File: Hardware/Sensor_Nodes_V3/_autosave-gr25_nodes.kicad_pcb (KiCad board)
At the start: 4 copper layers, 22.1 x 70 mm, 72 parts, among them J1 Conn_01x06_Socket, J2 Conn_01x27_Socket, J3 Conn_01x27_Socket, Q1 S9013, U1 STM32F103C8Tx, U2 STM32G474RBTx, U3 MCP2542FDxMF, U4 MCP2542FDxMF, U5 AMS1117-3.3, U6 TPS563200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

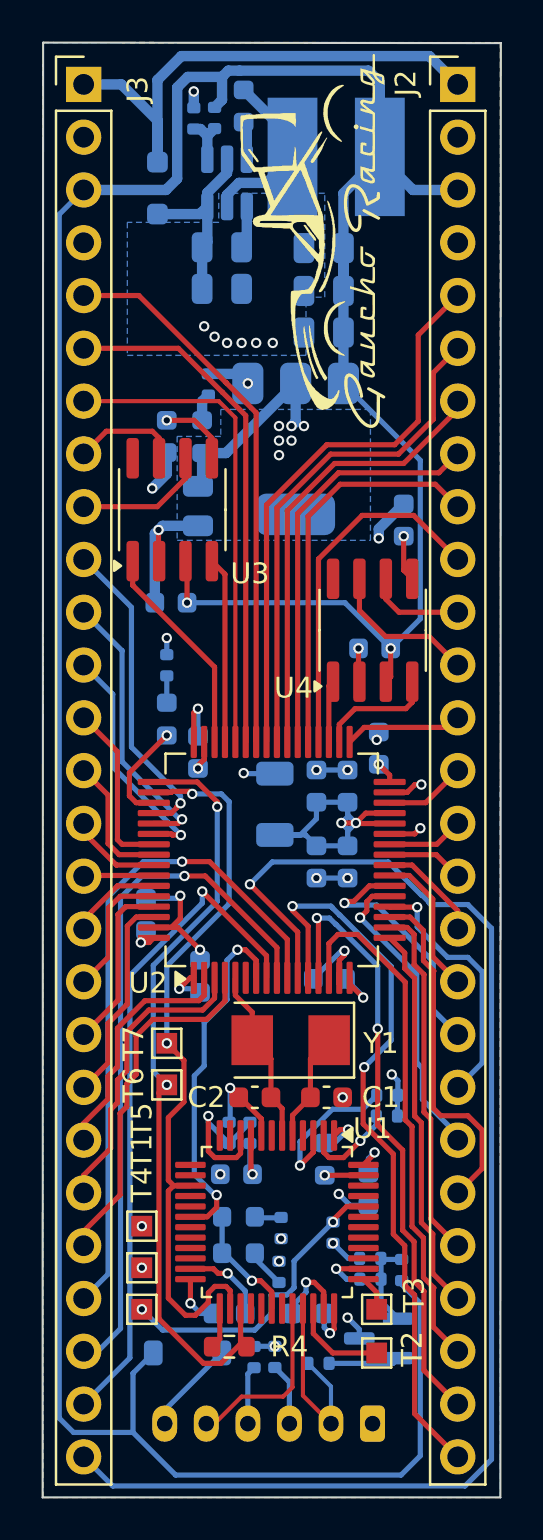
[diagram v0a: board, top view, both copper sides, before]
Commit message: rerouted a little and added swo
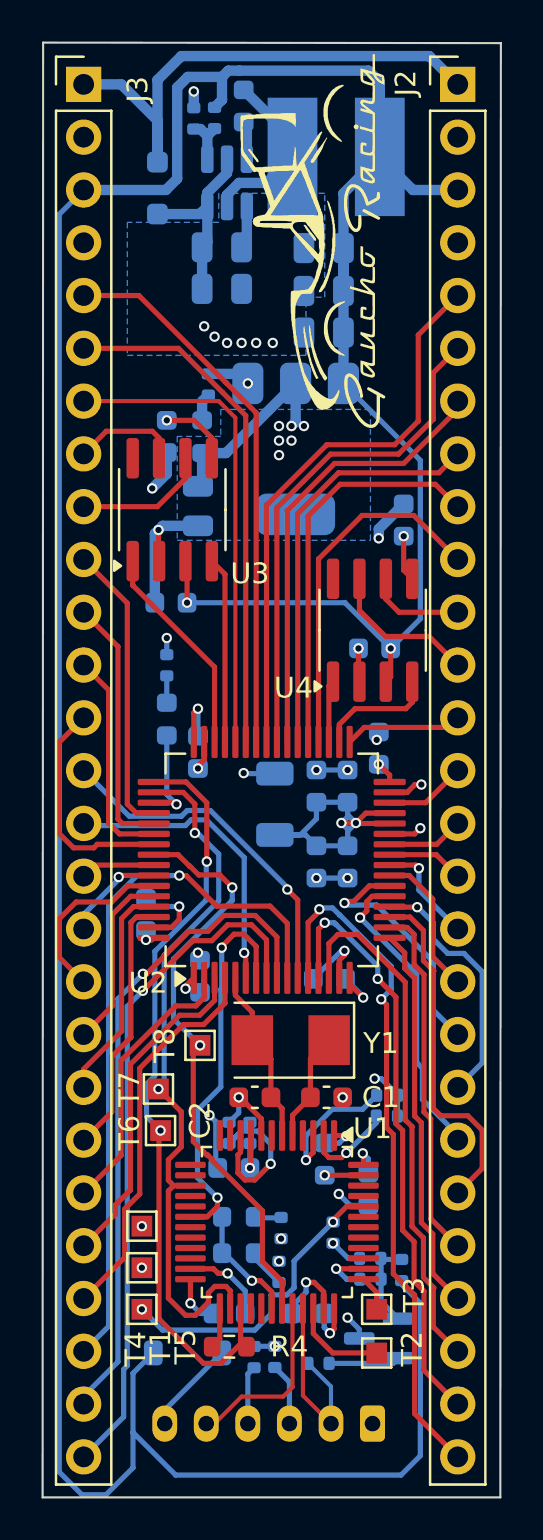
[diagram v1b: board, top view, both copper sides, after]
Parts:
- added T8: ~, TestPoint:TestPoint_Pad_1.0x1.0mm, F.Cu at (116.3, 76.0)
- moved T7 2.24 mm to (114.3, 78.1)
- moved T6 2.22 mm to (114.4, 80.1)
- moved C4 0.32 mm to (117.9, 81.9)
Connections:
- J3 pad 14: PB3 -> PC3
- J3 pad 15: PB4 -> PF1
- J3 pad 16: PB5 -> PB4
- J3 pad 17: PB6 -> PB5
- J3 pad 18: I2C1_SDA -> PB6
- J3 pad 19: I2C1_SCL -> I2C1_SDA
- J3 pad 20: PB9 -> I2C1_SCL
- J3 pad 21: PC13 -> PB9
- J3 pad 22: PC14 -> PC13
- J3 pad 23: PC15 -> PC14
- J3 pad 24: PC2 -> PC15
- J3 pad 25: PC1 -> PC2
- J3 pad 26: PC0 -> PC1
- J3 pad 27: PC3 -> PC0
- U1 pad 31: unconnected-(U1-PA10-Pad31) -> T_SWO
- U2 pad 56: PB3 -> T_SWO
- U2 pad 6: unconnected-(U2-PF1-Pad6) -> PF1
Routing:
- net PC3: track 65.2 -> 16.9 mm
- net T_SWO: track 0.00 -> 28.3 mm, vias 0 -> 2
- net PF1: track 0.00 -> 14.5 mm, vias 0 -> 1
- net PB3: track 6.42 -> 0.00 mm
- net +5V: track 163.6 -> 168.6 mm
- net PB6: track 4.50 -> 8.72 mm
- net PD2: track 8.38 -> 11.0 mm
- net PB9: track 10.1 -> 12.6 mm
- net +3.3V: track 40.4 -> 38.0 mm
- net I2C1_SCL: track 8.34 -> 10.7 mm
- net PA0: track 35.8 -> 33.5 mm
- net I2C1_SDA: track 6.46 -> 8.71 mm
- net PC2: track 32.5 -> 34.8 mm
- net PC1: track 33.8 -> 31.9 mm
- net PC13: track 11.7 -> 13.3 mm
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- added copper zone on In1.Cu, net +3.3V
- added copper zone on In1.Cu, net CANH2
- added copper zone on In2.Cu, net GND
- removed copper zone on B.Cu, net (none)
- removed copper zone on F.Cu, net (none)
- removed copper zone on In2.Cu, net +3.3V
- removed copper zone on In1.Cu, net GND
